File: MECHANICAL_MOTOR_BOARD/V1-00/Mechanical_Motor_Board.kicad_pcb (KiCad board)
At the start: 2 copper layers, 88.9 x 44.5 mm, 82 parts, among them K1 COLONETTE, K2 COLONETTE, K3 COLONETTE, K4 COLONETTE, P1001 CONN_02X13, P1002 CONN_02X08, P1003 CONN_01X02, P1004 CONN_01X02, P1005 CONN_01X04, P1006 CONN_01X04, Q3001 2N7002, Q3002 2N7002, Q3003 BSR14, Q3004 BSR14, Q3005 BTS50055, Q3006 BTS50055, Q3007 STB80NF55L_06T4, Q3008 STB80NF55L_06T4, Q3009 STB80NF55L_06T4, Q3010 STB80NF55L_06T4, Q3011 BTS50055, Q3012 BTS50055, Q3013 BSR14, Q3014 BSR14, Q3015 2N7002, Q3016 2N7002, U2001 HCTL-2032, U2002 M74VHC1GT02DTT1G, U3001 74HC02, U3002 74HC02, X2001 12Mhz

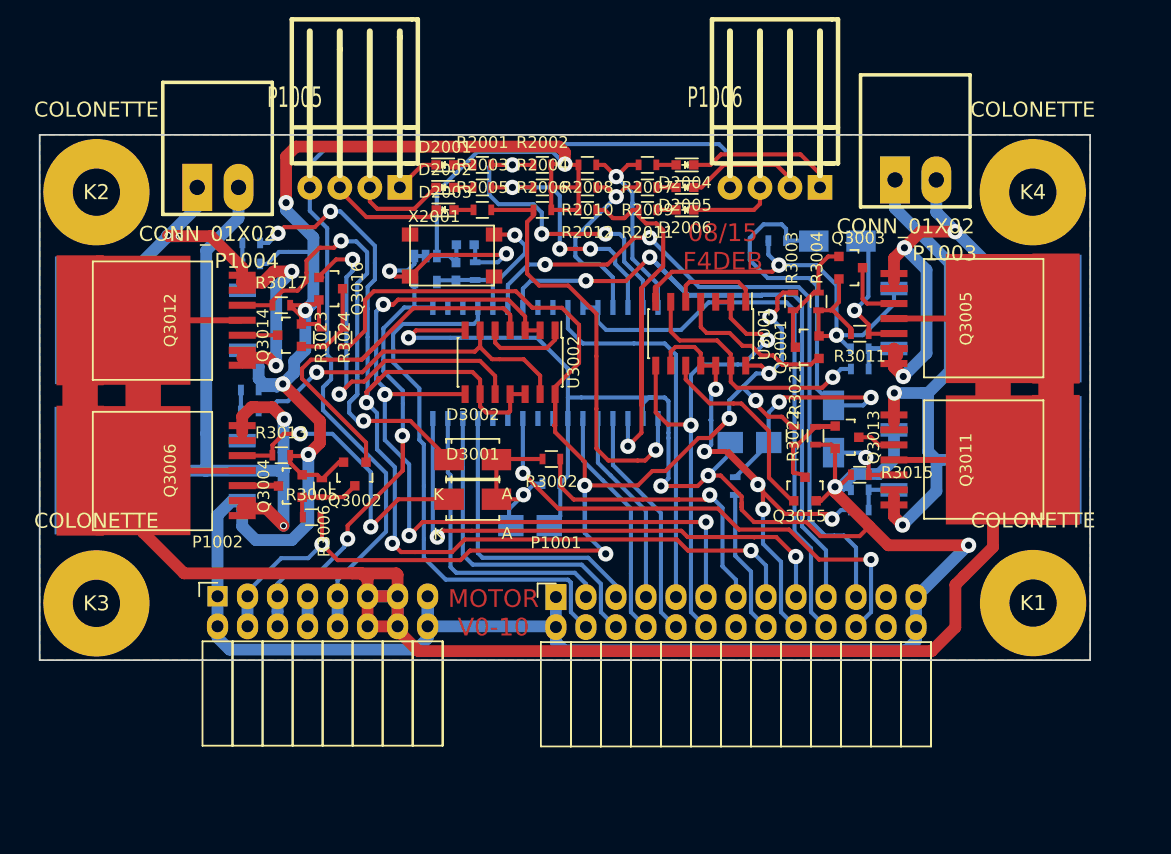
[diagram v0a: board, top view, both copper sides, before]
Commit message: test mechanicalmotorboard PCB NOK
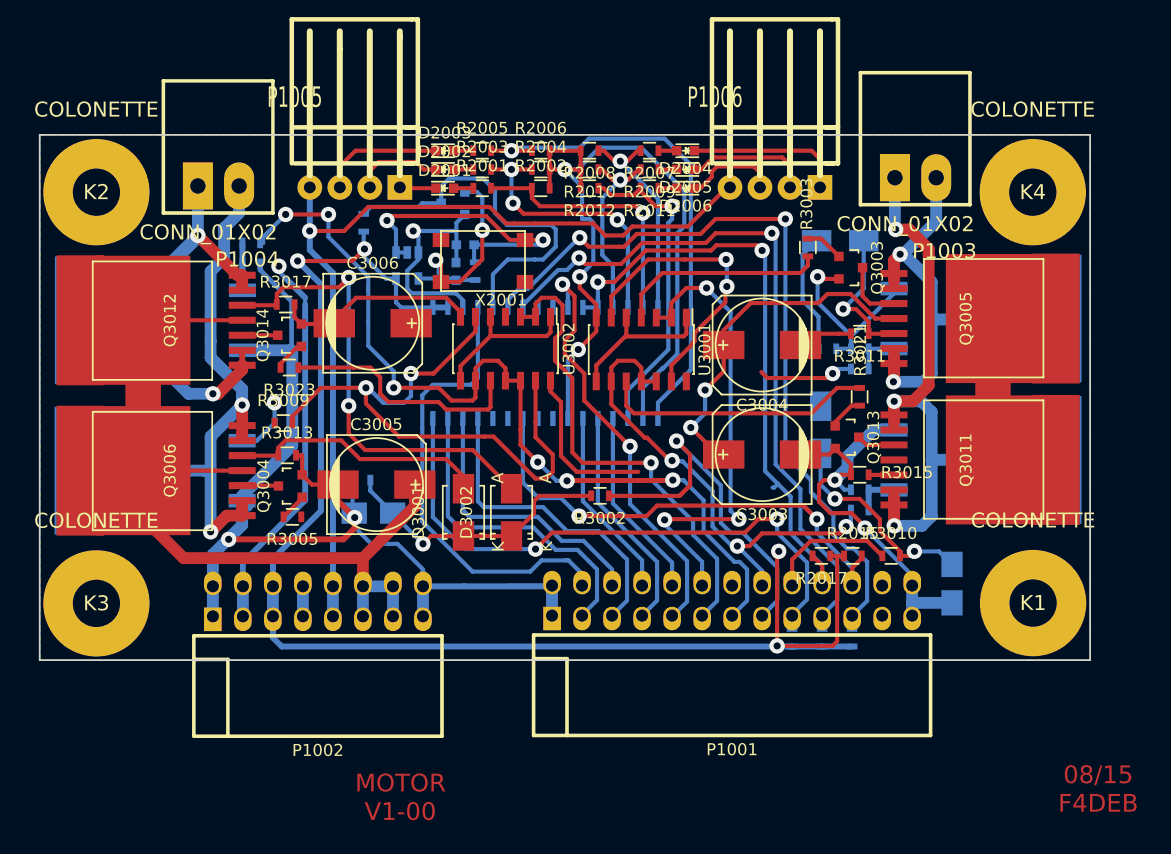
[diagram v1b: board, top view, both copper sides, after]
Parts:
- removed Q3001, Q3002, Q3015, Q3016: 2N7002, SOT-23
- removed R3004, R3006, R3022, R3024: R, Resistors_SMD:R_0603
- added C3003: 470U, c_elec_8x10.5, F.Cu at (175.4, 112.7)
- added C3004: CP, c_elec_8x10.5, F.Cu at (175.4, 103.4)
- added C3005: CP, c_elec_8x10.5, F.Cu at (142.7, 115.3)
- added C3006: CP, c_elec_8x10.5, F.Cu at (142.4, 101.6)
- added Q2001: 2N7002, Housings_SOT-23_SOT-143_TSOT-6:SOT-23, B.Cu at (149.2, 91.4)
- added R2014: 10k, Resistors_SMD:R_0603, B.Cu at (183.0, 128.2)
- added R2015: 10k, Resistors_SMD:R_0603, F.Cu at (183.1, 121.3)
- added R2016: 10k, Resistors_SMD:R_0603, B.Cu at (180.5, 128.2)
- added R2017: 10k, Resistors_SMD:R_0603, F.Cu at (180.4, 121.3)
- added R2018: 10k, Resistors_SMD:R_0603, B.Cu at (177.9, 128.2)
- added R2019: 1k, Resistors_SMD:R_0603, B.Cu at (141.7, 93.1)
- C3001, C3002: value C -> 10u
- D3001, D3002, D3003, D3004: value D_Schottky_Small -> B140
- P1001: footprint Socket_Strips:Socket_Strip_Angled_2x13 -> w_pin_strip:pin_socket_13x2-90
- P1002: footprint Socket_Strips:Socket_Strip_Angled_2x08 -> w_pin_strip:pin_socket_8x2-90
- Q3003, Q3004, Q3013, Q3014: footprint SOT-23 -> Housings_SOT-23_SOT-143_TSOT-6:SOT-23
- R2001, R2002, R2003, R2004, R2005, R2006, R2007, R2008, R2009, R2010, R2011, R2012: value 1.5k -> 2.1k
- R3001, R3007, R3012, R3014, R3016, R3018: value R -> 100k
- R3002, R3003, R3005, R3021, R3023: value R -> 10k
- R3008, R3019, R3020: value R -> 100
- R3009: value R -> 100; moved to F.Cu
- R3010: value R -> 10k; moved to F.Cu
- R3011, R3013, R3015, R3017: value R -> 2.2k
- moved C3002 20.9 mm to (191.5, 123.6), turned to 270 degrees
- moved R3001 16.1 mm to (141.5, 114.9), turned to 0 degrees
- moved P1001 15.8 mm to (172.8, 130.0)
- moved R3010 14.5 mm to (186.3, 121.3), turned to 0 degrees
- moved C3001 13.3 mm to (142.5, 117.7), turned to 180 degrees
- moved R3007 10.1 mm to (180.9, 103.8), turned to 180 degrees
- moved P1002 10.0 mm to (137.8, 130.0)
- moved R3021 6.42 mm to (183.6, 107.8)
- moved D3002 5.54 mm to (154.2, 117.6), turned to 90 degrees
- moved R3023 5.24 mm to (135.4, 105.3), turned to 180 degrees
- moved U3001 5.20 mm to (165.2, 103.8)
- moved R3002 5.16 mm to (161.7, 116.2)
- moved R2006 5.01 mm to (156.7, 87.0)
- moved D2003 5.01 mm to (148.5, 87.0)
- moved R2005 5.01 mm to (151.7, 87.0)
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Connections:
- D3001 pad 1: /Motor/IMOT2A -> Net-(C3001-Pad1)
- D3001 pad 2: Net-(C3001-Pad1) -> /Motor/IMOT2A
- D3002 pad 1: /Motor/IMOT2B -> Net-(C3001-Pad1)
- D3002 pad 2: Net-(C3001-Pad1) -> /Motor/IMOT2B
- D3003 pad 1: /Motor/IMOT1A -> Net-(C3002-Pad1)
- D3003 pad 2: Net-(C3002-Pad1) -> /Motor/IMOT1A
- D3004 pad 1: /Motor/IMOT1B -> Net-(C3002-Pad1)
- D3004 pad 2: Net-(C3002-Pad1) -> /Motor/IMOT1B
- P1001 pad 13: /Motor/IMOT2 -> /Motor/IO9
- P1001 pad 15: /Motor/IO7 -> /Motor/IMOT2
- P1001 pad 16: /Motor/IMOT1 -> /Motor/IO8
- P1001 pad 18: /Motor/IO6 -> /Motor/IMOT1
- Q3003 pad 1: Net-(Q3001-Pad3) -> Net-(Q3003-Pad1)
- Q3004 pad 1: Net-(Q3002-Pad3) -> Net-(Q3004-Pad1)
- R3003 pad 1: Net-(Q3001-Pad3) -> Net-(R3003-Pad1)
- R3003 pad 2: +3V3 -> Net-(Q3003-Pad1)
- R3005 pad 1: Net-(Q3002-Pad3) -> Net-(R3005-Pad1)
- R3005 pad 2: +3V3 -> Net-(Q3004-Pad1)
- R3019 pad 2: /Motor/IO6 -> /Motor/IO8
- R3020 pad 2: /Motor/IO7 -> /Motor/IO9
- R3021 pad 1: +3V3 -> Net-(R3021-Pad1)
- R3023 pad 1: +3V3 -> Net-(R3023-Pad1)
- U2001 pad 2: (no net) -> +5VD
- U2001 pad 3: (no net) -> GND
- U2001 pad 5: Net-(C2002-Pad1) -> Net-(Q2001-Pad3)
- U3001 pad 10: Net-(Q3015-Pad1) -> Net-(R3021-Pad1)
- U3001 pad 11: /Motor/IO6 -> /Motor/IO8
- U3001 pad 12: /Motor/IO6 -> /Motor/IO8
- U3001 pad 4: Net-(Q3001-Pad1) -> Net-(R3003-Pad1)
- U3001 pad 8: /Motor/OC5-5V -> Net-(U3001-Pad1)
- U3001 pad 9: /Motor/IO6 -> /Motor/IO8
- U3002 pad 10: Net-(Q3016-Pad1) -> Net-(R3023-Pad1)
- U3002 pad 11: /Motor/IO7 -> /Motor/IO9
- U3002 pad 12: /Motor/IO7 -> /Motor/IO9
- U3002 pad 4: Net-(Q3002-Pad1) -> Net-(R3005-Pad1)
- U3002 pad 8: /Motor/OC4-5V -> Net-(U3002-Pad1)
- U3002 pad 9: /Motor/IO7 -> /Motor/IO9
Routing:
- net GND: track 395.7 -> 278.3 mm, vias 12 -> 9
- net /Motor/IO7: track 95.6 -> 0.00 mm, vias 5 -> 0
- net +15V: track 211.7 -> 118.0 mm, vias 0 -> 2
- net +3V3: track 132.9 -> 48.8 mm, vias 7 -> 1
- net /Motor/IO9: track 0.00 -> 83.7 mm, vias 0 -> 6
- net +5VD: track 41.9 -> 125.1 mm, vias 2 -> 4
- net /Motor/IO6: track 52.1 -> 0.00 mm, vias 5 -> 0
- net /Motor/IO8: track 0.00 -> 41.6 mm, vias 0 -> 3
- net Net-(Q3002-Pad1): track 34.9 -> 0.00 mm
- net /Motor/OC4-5V: track 75.8 -> 41.3 mm, vias 4 -> 1
- net Net-(Q3016-Pad1): track 32.1 -> 0.00 mm, vias 2 -> 0
- net Net-(Q2001-Pad3): track 0.00 -> 31.8 mm
- net Net-(R3021-Pad1): track 0.00 -> 23.0 mm
- net Net-(R3023-Pad1): track 0.00 -> 20.9 mm
- net Net-(R3009-Pad2): track 30.1 -> 50.8 mm, vias 1 -> 2
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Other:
- board text added: "MOTOR V1-00"
- board text removed: "MOTOR V0-10"

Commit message: New Beacon_Main_Board
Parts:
- removed C3004, C3006: CP, c_elec_8x10.5
- C3003, C3005: footprint c_elec_8x10.5 -> Capacitors_ThroughHole:C_Axial_D13_L31_P38
- R3005: footprint Resistors_SMD:R_0603 -> Resistors_SMD:R_0805
- R3009: moved to B.Cu
- R3019, U2002: moved to F.Cu
- R3021: footprint Resistors_SMD:R_0603 -> Resistors_SMD:R_1206
- moved C3003 38.4 mm to (139.3, 99.4), turned to 0 degrees
- moved R3002 11.8 mm to (172.4, 121.0)
- moved R3001 9.60 mm to (148.8, 121.0)
- moved R3021 6.90 mm to (176.8, 107.1), turned to 0 degrees
- moved U2002 6.33 mm to (139.2, 95.2)
- moved C3001 5.72 mm to (148.2, 117.5)
- moved U2001 4.81 mm to (161.8, 105.7)
- moved C3005 3.95 mm to (139.3, 113.3)
- moved R3023 3.48 mm to (138.7, 104.5)
- moved U3001 3.02 mm to (167.5, 105.7), turned to 0 degrees
- moved D3004 2.87 mm to (181.7, 108.1), turned to 180 degrees
- moved D3002 2.54 mm to (154.2, 120.1)
- moved D3001 2.54 mm to (150.1, 120.1)
- moved R3003 2.22 mm to (181.2, 94.0), turned to 0 degrees
- moved X2001 1.84 mm to (149.9, 96.3)
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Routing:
- net +15V: track 118.0 -> 220.2 mm
- net Net-(R3005-Pad1): track 0.00 -> 53.8 mm, vias 0 -> 2
- net +3V3: track 48.8 -> 101.9 mm, vias 1 -> 3
- net GND: track 278.3 -> 322.6 mm, vias 9 -> 15
- net Net-(R2001-Pad2): track 22.2 -> 51.1 mm
- net /Motor/IMOT2: track 32.1 -> 9.34 mm
- net /Codeur/IO25: track 35.9 -> 56.6 mm
- net Net-(C2002-Pad1): track 20.0 -> 38.6 mm, vias 2 -> 1
- net Net-(R3009-Pad2): track 50.8 -> 32.3 mm, vias 2 -> 1
- net Net-(R3021-Pad1): track 23.0 -> 5.15 mm
- net Net-(U3002-Pad1): track 13.0 -> 27.3 mm, vias 0 -> 2
- net /Motor/OC5-5V: track 40.0 -> 54.0 mm, vias 3 -> 1
- net /Motor/IMOT1B: track 2.15 -> 15.3 mm, vias 0 -> 3
- net /Motor/IMOT2B: track 39.4 -> 51.6 mm, vias 2 -> 4
- net +12V: track 76.2 -> 88.2 mm, vias 1 -> 2
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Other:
- board text added: "10/15"
- board text added: "MOTOR"
- board text added: "V1-00"
- board text removed: "08/15 F4DEB"

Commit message: MAJ 2018
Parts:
- added C2001: 27p, Capacitors_SMD:C_0603, F.Cu at (73.3, 164.6)
- added C2001: 27p, Capacitors_SMD:C_0603, F.Cu at (73.8, 71.9)
- added C2001: 27p, Capacitors_SMD:C_0603, B.Cu at (208.7, 138.6)
- added C2002: 27p, Capacitors_SMD:C_0603, F.Cu at (72.5, 162.4)
- added C2002: 27p, Capacitors_SMD:C_0603, F.Cu at (73.0, 69.7)
- added C2002: 27p, Capacitors_SMD:C_0603, B.Cu at (207.9, 140.9)
- added C3001: 10u, Capacitors_Tantalum_SMD:TantalC_SizeB_EIA-3528_Wave, F.Cu at (71.2, 142.1)
- added C3001: 10u, Capacitors_Tantalum_SMD:TantalC_SizeB_EIA-3528_Wave, F.Cu at (71.8, 49.4)
- added C3001: 10u, Capacitors_Tantalum_SMD:TantalC_SizeB_EIA-3528_Wave, B.Cu at (206.6, 161.2)
- added C3002: 10u, Capacitors_Tantalum_SMD:TantalC_SizeB_EIA-3528_Wave, F.Cu at (114.5, 136.0)
- added C3002: 10u, Capacitors_Tantalum_SMD:TantalC_SizeB_EIA-3528_Wave, F.Cu at (115.0, 43.2)
- added C3002: 10u, Capacitors_Tantalum_SMD:TantalC_SizeB_EIA-3528_Wave, B.Cu at (249.9, 167.3)
- added C3003: 470U, Capacitors_ThroughHole:C_Axial_D13_L31_P38, B.Cu at (62.4, 160.1)
- added C3003: 470U, Capacitors_ThroughHole:C_Axial_D13_L31_P38, B.Cu at (62.9, 67.4)
- added C3003: 470U, Capacitors_ThroughHole:C_Axial_D13_L31_P38, F.Cu at (197.7, 143.1)
- added C3005: CP, Capacitors_ThroughHole:C_Axial_D13_L31_P38, B.Cu at (62.4, 146.3)
- added C3005: CP, Capacitors_ThroughHole:C_Axial_D13_L31_P38, B.Cu at (62.9, 53.6)
- added C3005: CP, Capacitors_ThroughHole:C_Axial_D13_L31_P38, F.Cu at (197.7, 157.0)
- added D2001: LED, LEDs:LED-0603, B.Cu at (71.6, 169.4)
- added D2001: LED, LEDs:LED-0603, B.Cu at (72.1, 76.7)
- added D2001: LED, LEDs:LED-0603, F.Cu at (206.9, 133.9)
- added D2002: LED, LEDs:LED-0603, B.Cu at (71.6, 171.0)
- added D2002: LED, LEDs:LED-0603, B.Cu at (72.1, 78.3)
- added D2002: LED, LEDs:LED-0603, F.Cu at (206.9, 132.3)
- added D2003: LED, LEDs:LED-0603, B.Cu at (71.6, 172.6)
- added D2003: LED, LEDs:LED-0603, B.Cu at (72.1, 79.9)
- added D2003: LED, LEDs:LED-0603, F.Cu at (206.9, 130.7)
- added D2004: LED, LEDs:LED-0603, B.Cu at (91.9, 172.6)
- added D2004: LED, LEDs:LED-0603, B.Cu at (92.5, 79.9)
- added D2004: LED, LEDs:LED-0603, F.Cu at (227.3, 130.7)
- added D2005: LED, LEDs:LED-0603, B.Cu at (91.9, 171.0)
- added D2005: LED, LEDs:LED-0603, B.Cu at (92.5, 78.3)
- added D2005: LED, LEDs:LED-0603, F.Cu at (227.3, 132.3)
- added D2006: LED, LEDs:LED-0603, B.Cu at (91.9, 169.4)
- added D2006: LED, LEDs:LED-0603, B.Cu at (92.5, 76.7)
- added D2006: LED, LEDs:LED-0603, F.Cu at (227.3, 133.9)
- added D3001: B140, Diodes_SMD:Diode-SMA_Standard, B.Cu at (73.2, 139.4)
- added D3001: B140, Diodes_SMD:Diode-SMA_Standard, B.Cu at (73.7, 46.7)
- added D3001: B140, Diodes_SMD:Diode-SMA_Standard, F.Cu at (208.5, 163.8)
- added D3002: B140, Diodes_SMD:Diode-SMA_Standard, B.Cu at (77.3, 139.4)
- added D3002: B140, Diodes_SMD:Diode-SMA_Standard, B.Cu at (77.8, 46.7)
- added D3002: B140, Diodes_SMD:Diode-SMA_Standard, F.Cu at (212.7, 163.8)
- added D3003: B140, Diodes_SMD:Diode-SMA_Standard, F.Cu at (104.9, 164.9)
- added D3003: B140, Diodes_SMD:Diode-SMA_Standard, F.Cu at (105.4, 72.2)
- added D3003: B140, Diodes_SMD:Diode-SMA_Standard, B.Cu at (240.3, 138.4)
- added D3004: B140, Diodes_SMD:Diode-SMA_Standard, F.Cu at (104.7, 151.5)
- added D3004: B140, Diodes_SMD:Diode-SMA_Standard, F.Cu at (105.2, 58.8)
- added D3004: B140, Diodes_SMD:Diode-SMA_Standard, B.Cu at (240.1, 151.8)
- added K1: COLONETTE, CEN-PCB:COLONETTE, B.Cu at (121.4, 134.3)
- added K1: COLONETTE, CEN-PCB:COLONETTE, B.Cu at (121.9, 41.6)
- added K1: COLONETTE, CEN-PCB:COLONETTE, F.Cu at (256.7, 169.0)
- added K2: COLONETTE, CEN-PCB:COLONETTE, B.Cu at (42.1, 169.1)
- added K2: COLONETTE, CEN-PCB:COLONETTE, B.Cu at (42.6, 76.4)
- added K2: COLONETTE, CEN-PCB:COLONETTE, F.Cu at (177.5, 134.2)
- added K3: COLONETTE, CEN-PCB:COLONETTE, B.Cu at (42.1, 134.3)
- added K3: COLONETTE, CEN-PCB:COLONETTE, B.Cu at (42.6, 41.6)
- added K3: COLONETTE, CEN-PCB:COLONETTE, F.Cu at (177.5, 169.0)
- added K4: COLONETTE, CEN-PCB:COLONETTE, B.Cu at (121.3, 169.1)
- added K4: COLONETTE, CEN-PCB:COLONETTE, B.Cu at (121.8, 76.4)
- added K4: COLONETTE, CEN-PCB:COLONETTE, F.Cu at (256.7, 134.2)
- added P1001: CONN_02X13, w_pin_strip:pin_socket_13x2-90, B.Cu at (95.9, 129.6)
- added P1001: CONN_02X13, w_pin_strip:pin_socket_13x2-90, B.Cu at (96.4, 36.9)
- added P1001: CONN_02X13, w_pin_strip:pin_socket_13x2-90, F.Cu at (231.3, 173.7)
- added P1002: CONN_02X08, w_pin_strip:pin_socket_8x2-90, B.Cu at (60.8, 129.5)
- added P1002: CONN_02X08, w_pin_strip:pin_socket_8x2-90, B.Cu at (61.3, 36.8)
- added P1002: CONN_02X08, w_pin_strip:pin_socket_8x2-90, F.Cu at (196.2, 173.7)
- added P1003: CONN_01X02, CEN-PCB:WEIDMULLER-SL-3.5-2-90G, B.Cu at (109.7, 170.3)
- added P1003: CONN_01X02, CEN-PCB:WEIDMULLER-SL-3.5-2-90G, B.Cu at (110.2, 77.6)
- added P1003: CONN_01X02, CEN-PCB:WEIDMULLER-SL-3.5-2-90G, F.Cu at (245.0, 133.0)
- added P1004: CONN_01X02, CEN-PCB:WEIDMULLER-SL-3.5-2-90G, B.Cu at (50.7, 169.6)
- added P1004: CONN_01X02, CEN-PCB:WEIDMULLER-SL-3.5-2-90G, B.Cu at (51.2, 76.9)
- added P1004: CONN_01X02, CEN-PCB:WEIDMULLER-SL-3.5-2-90G, F.Cu at (186.1, 133.7)
- added P1005: CONN_01X04, CEN-PCB:KK-4-H, B.Cu at (60.1, 169.5)
- added P1005: CONN_01X04, CEN-PCB:KK-4-H, B.Cu at (60.7, 76.8)
- added P1005: CONN_01X04, CEN-PCB:KK-4-H, F.Cu at (195.5, 133.8)
- added P1006: CONN_01X04, CEN-PCB:KK-4-H, B.Cu at (95.7, 169.5)
- added P1006: CONN_01X04, CEN-PCB:KK-4-H, B.Cu at (96.2, 76.8)
- added P1006: CONN_01X04, CEN-PCB:KK-4-H, F.Cu at (231.1, 133.8)
- added Q2001: 2N7002, Housings_SOT-23_SOT-143_TSOT-6:SOT-23, F.Cu at (72.3, 168.1)
- added Q2001: 2N7002, Housings_SOT-23_SOT-143_TSOT-6:SOT-23, F.Cu at (72.8, 75.4)
- added Q2001: 2N7002, Housings_SOT-23_SOT-143_TSOT-6:SOT-23, B.Cu at (207.6, 135.1)
- added Q3003: BSR14, Housings_SOT-23_SOT-143_TSOT-6:SOT-23, B.Cu at (105.9, 162.7)
- added Q3003: BSR14, Housings_SOT-23_SOT-143_TSOT-6:SOT-23, B.Cu at (106.4, 70.0)
- added Q3003: BSR14, Housings_SOT-23_SOT-143_TSOT-6:SOT-23, F.Cu at (241.3, 140.6)
- added Q3004: BSR14, Housings_SOT-23_SOT-143_TSOT-6:SOT-23, B.Cu at (58.5, 143.9)
- added Q3004: BSR14, Housings_SOT-23_SOT-143_TSOT-6:SOT-23, B.Cu at (59.0, 51.2)
- added Q3004: BSR14, Housings_SOT-23_SOT-143_TSOT-6:SOT-23, F.Cu at (193.9, 159.4)
- added Q3005: BTS50055, f4deb-mod-library:PG-TO220-7-4, B.Cu at (109.6, 158.4)
- added Q3005: BTS50055, f4deb-mod-library:PG-TO220-7-4, B.Cu at (110.1, 65.7)
- added Q3005: BTS50055, f4deb-mod-library:PG-TO220-7-4, F.Cu at (245.0, 144.9)
- added Q3006: BTS50055, f4deb-mod-library:PG-TO220-7-4, B.Cu at (54.4, 145.5)
- added Q3006: BTS50055, f4deb-mod-library:PG-TO220-7-4, B.Cu at (54.9, 52.8)
- added Q3006: BTS50055, f4deb-mod-library:PG-TO220-7-4, F.Cu at (189.8, 157.8)
- added Q3007: STB80NF55L_06T4, SMD_Packages:TO-263, F.Cu at (109.6, 158.4)
- added Q3007: STB80NF55L_06T4, SMD_Packages:TO-263, F.Cu at (110.1, 65.7)
- added Q3007: STB80NF55L_06T4, SMD_Packages:TO-263, B.Cu at (245.0, 144.9)
- added Q3008: STB80NF55L_06T4, SMD_Packages:TO-263, F.Cu at (54.4, 145.5)
- added Q3008: STB80NF55L_06T4, SMD_Packages:TO-263, F.Cu at (54.9, 52.8)
- added Q3008: STB80NF55L_06T4, SMD_Packages:TO-263, B.Cu at (189.8, 157.8)
- added Q3009: STB80NF55L_06T4, SMD_Packages:TO-263, F.Cu at (109.6, 146.4)
- added Q3009: STB80NF55L_06T4, SMD_Packages:TO-263, F.Cu at (110.1, 53.7)
- added Q3009: STB80NF55L_06T4, SMD_Packages:TO-263, B.Cu at (245.0, 156.9)
- added Q3010: STB80NF55L_06T4, SMD_Packages:TO-263, F.Cu at (54.4, 158.2)
- added Q3010: STB80NF55L_06T4, SMD_Packages:TO-263, F.Cu at (55.0, 65.5)
- added Q3010: STB80NF55L_06T4, SMD_Packages:TO-263, B.Cu at (189.8, 145.0)
- added Q3011: BTS50055, f4deb-mod-library:PG-TO220-7-4, B.Cu at (109.6, 146.4)
- added Q3011: BTS50055, f4deb-mod-library:PG-TO220-7-4, B.Cu at (110.1, 53.7)
- added Q3011: BTS50055, f4deb-mod-library:PG-TO220-7-4, F.Cu at (245.0, 156.9)
- added Q3012: BTS50055, f4deb-mod-library:PG-TO220-7-4, B.Cu at (54.4, 158.2)
- added Q3012: BTS50055, f4deb-mod-library:PG-TO220-7-4, B.Cu at (54.9, 65.5)
- added Q3012: BTS50055, f4deb-mod-library:PG-TO220-7-4, F.Cu at (189.8, 145.0)
- added Q3013: BSR14, Housings_SOT-23_SOT-143_TSOT-6:SOT-23, B.Cu at (105.6, 148.3)
- added Q3013: BSR14, Housings_SOT-23_SOT-143_TSOT-6:SOT-23, B.Cu at (106.1, 55.6)
- added Q3013: BSR14, Housings_SOT-23_SOT-143_TSOT-6:SOT-23, F.Cu at (241.0, 154.9)
- added Q3014: BSR14, Housings_SOT-23_SOT-143_TSOT-6:SOT-23, B.Cu at (58.5, 156.1)
- added Q3014: BSR14, Housings_SOT-23_SOT-143_TSOT-6:SOT-23, B.Cu at (59.0, 63.4)
- added Q3014: BSR14, Housings_SOT-23_SOT-143_TSOT-6:SOT-23, F.Cu at (193.9, 147.2)
- added R2001: 2.1k, Resistors_SMD:R_0603, B.Cu at (74.7, 169.4)
- added R2001: 2.1k, Resistors_SMD:R_0603, B.Cu at (75.2, 76.7)
- added R2001: 2.1k, Resistors_SMD:R_0603, F.Cu at (210.1, 133.9)
- added R2002: 2.1k, Resistors_SMD:R_0603, B.Cu at (79.7, 169.4)
- added R2002: 2.1k, Resistors_SMD:R_0603, B.Cu at (80.2, 76.7)
- added R2002: 2.1k, Resistors_SMD:R_0603, F.Cu at (215.1, 133.9)
- added R2003: 2.1k, Resistors_SMD:R_0603, B.Cu at (74.7, 171.0)
- added R2003: 2.1k, Resistors_SMD:R_0603, B.Cu at (75.2, 78.3)
- added R2003: 2.1k, Resistors_SMD:R_0603, F.Cu at (210.1, 132.3)
- added R2004: 2.1k, Resistors_SMD:R_0603, B.Cu at (79.7, 171.0)
- added R2004: 2.1k, Resistors_SMD:R_0603, B.Cu at (80.2, 78.3)
- added R2004: 2.1k, Resistors_SMD:R_0603, F.Cu at (215.1, 132.3)
- added R2005: 2.1k, Resistors_SMD:R_0603, B.Cu at (74.7, 172.6)
- added R2005: 2.1k, Resistors_SMD:R_0603, B.Cu at (75.2, 79.9)
- added R2005: 2.1k, Resistors_SMD:R_0603, F.Cu at (210.1, 130.7)
- added R2006: 2.1k, Resistors_SMD:R_0603, B.Cu at (79.7, 172.6)
- added R2006: 2.1k, Resistors_SMD:R_0603, B.Cu at (80.2, 79.9)
- added R2006: 2.1k, Resistors_SMD:R_0603, F.Cu at (215.1, 130.7)
- added R2007: 2.1k, Resistors_SMD:R_0603, B.Cu at (88.9, 172.6)
- added R2007: 2.1k, Resistors_SMD:R_0603, B.Cu at (89.4, 79.9)
- added R2007: 2.1k, Resistors_SMD:R_0603, F.Cu at (224.3, 130.7)
- added R2008: 2.1k, Resistors_SMD:R_0603, B.Cu at (83.8, 172.6)
- added R2008: 2.1k, Resistors_SMD:R_0603, B.Cu at (84.3, 79.9)
- added R2008: 2.1k, Resistors_SMD:R_0603, F.Cu at (219.2, 130.7)
- added R2009: 2.1k, Resistors_SMD:R_0603, B.Cu at (88.9, 171.0)
- added R2009: 2.1k, Resistors_SMD:R_0603, B.Cu at (89.4, 78.3)
- added R2009: 2.1k, Resistors_SMD:R_0603, F.Cu at (224.3, 132.3)
- added R2010: 2.1k, Resistors_SMD:R_0603, B.Cu at (83.8, 171.0)
- added R2010: 2.1k, Resistors_SMD:R_0603, B.Cu at (84.3, 78.3)
- added R2010: 2.1k, Resistors_SMD:R_0603, F.Cu at (219.2, 132.3)
- added R2011: 2.1k, Resistors_SMD:R_0603, B.Cu at (88.9, 169.4)
- added R2011: 2.1k, Resistors_SMD:R_0603, B.Cu at (89.4, 76.7)
- added R2011: 2.1k, Resistors_SMD:R_0603, F.Cu at (224.3, 133.9)
- added R2012: 2.1k, Resistors_SMD:R_0603, B.Cu at (83.8, 169.4)
- added R2012: 2.1k, Resistors_SMD:R_0603, B.Cu at (84.3, 76.7)
- added R2012: 2.1k, Resistors_SMD:R_0603, F.Cu at (219.2, 133.9)
- added R2013: 10M, Resistors_SMD:R_0603, F.Cu at (74.1, 162.4)
- added R2013: 10M, Resistors_SMD:R_0603, F.Cu at (74.6, 69.7)
- added R2013: 10M, Resistors_SMD:R_0603, B.Cu at (209.5, 140.9)
- added R2014: 10k, Resistors_SMD:R_0603, F.Cu at (106.0, 131.4)
- added R2014: 10k, Resistors_SMD:R_0603, F.Cu at (106.6, 38.7)
- added R2014: 10k, Resistors_SMD:R_0603, B.Cu at (241.4, 171.9)
- added R2015: 10k, Resistors_SMD:R_0603, B.Cu at (106.8, 138.3)
- added R2015: 10k, Resistors_SMD:R_0603, B.Cu at (107.3, 45.6)
- added R2015: 10k, Resistors_SMD:R_0603, F.Cu at (242.2, 165.0)
- added R2016: 10k, Resistors_SMD:R_0603, F.Cu at (103.5, 131.4)
- added R2016: 10k, Resistors_SMD:R_0603, F.Cu at (104.0, 38.7)
- added R2016: 10k, Resistors_SMD:R_0603, B.Cu at (238.9, 171.9)
- added R2017: 10k, Resistors_SMD:R_0603, B.Cu at (102.7, 138.3)
- added R2017: 10k, Resistors_SMD:R_0603, B.Cu at (103.3, 45.6)
- added R2017: 10k, Resistors_SMD:R_0603, F.Cu at (238.1, 165.0)
- added R2018: 10k, Resistors_SMD:R_0603, F.Cu at (101.0, 131.4)
- added R2018: 10k, Resistors_SMD:R_0603, F.Cu at (101.5, 38.7)
- added R2018: 10k, Resistors_SMD:R_0603, B.Cu at (236.3, 171.9)
- added R2019: 1k, Resistors_SMD:R_0603, F.Cu at (64.7, 166.5)
- added R2019: 1k, Resistors_SMD:R_0603, F.Cu at (65.2, 73.8)
- added R2019: 1k, Resistors_SMD:R_0603, B.Cu at (200.1, 136.8)
- added R3001: 100k, Resistors_SMD:R_0603, F.Cu at (71.9, 138.6)
- added R3001: 100k, Resistors_SMD:R_0603, F.Cu at (72.4, 45.8)
- added R3001: 100k, Resistors_SMD:R_0603, B.Cu at (207.3, 164.7)
- added R3002: 10k, Resistors_SMD:R_0603, B.Cu at (95.4, 138.6)
- added R3002: 10k, Resistors_SMD:R_0603, B.Cu at (95.9, 45.8)
- added R3002: 10k, Resistors_SMD:R_0603, F.Cu at (230.8, 164.7)
- added R3003: 10k, Resistors_SMD:R_0603, B.Cu at (104.2, 165.5)
- added R3003: 10k, Resistors_SMD:R_0603, B.Cu at (104.7, 72.8)
- added R3003: 10k, Resistors_SMD:R_0603, F.Cu at (239.6, 137.7)
- added R3005: 10k, Resistors_SMD:R_0805, B.Cu at (59.4, 140.6)
- added R3005: 10k, Resistors_SMD:R_0805, B.Cu at (59.9, 47.9)
- added R3005: 10k, Resistors_SMD:R_0805, F.Cu at (194.8, 162.7)
- added R3007: 100k, Resistors_SMD:R_0603, F.Cu at (103.9, 155.8)
- added R3007: 100k, Resistors_SMD:R_0603, F.Cu at (104.5, 63.1)
- added R3007: 100k, Resistors_SMD:R_0603, B.Cu at (239.3, 147.4)
- added R3008: 100, Resistors_SMD:R_0603, F.Cu at (106.7, 154.1)
- added R3008: 100, Resistors_SMD:R_0603, F.Cu at (107.2, 61.4)
- added R3008: 100, Resistors_SMD:R_0603, B.Cu at (242.1, 149.2)
- added R3009: 100, Resistors_SMD:R_0603, F.Cu at (58.7, 150.6)
- added R3009: 100, Resistors_SMD:R_0603, F.Cu at (59.2, 57.9)
- added R3009: 100, Resistors_SMD:R_0603, B.Cu at (194.1, 152.7)
- added R3010: 10k, Resistors_SMD:R_0603, B.Cu at (109.3, 138.3)
- added R3010: 10k, Resistors_SMD:R_0603, B.Cu at (109.9, 45.6)
- added R3010: 10k, Resistors_SMD:R_0603, F.Cu at (244.7, 165.0)
- added R3011: 2.2k, Resistors_SMD:R_0603, B.Cu at (106.7, 157.4)
- added R3011: 2.2k, Resistors_SMD:R_0603, B.Cu at (107.2, 64.6)
- added R3011: 2.2k, Resistors_SMD:R_0603, F.Cu at (242.1, 145.9)
- added R3012: 100k, Resistors_SMD:R_0603, F.Cu at (106.7, 155.8)
- added R3012: 100k, Resistors_SMD:R_0603, F.Cu at (107.2, 63.1)
- added R3012: 100k, Resistors_SMD:R_0603, B.Cu at (242.1, 147.4)
- added R3013: 2.2k, Resistors_SMD:R_0603, B.Cu at (58.7, 147.0)
- added R3013: 2.2k, Resistors_SMD:R_0603, B.Cu at (59.2, 54.3)
- added R3013: 2.2k, Resistors_SMD:R_0603, F.Cu at (194.1, 156.3)
- added R3014: 100k, Resistors_SMD:R_0603, F.Cu at (58.7, 148.8)
- added R3014: 100k, Resistors_SMD:R_0603, F.Cu at (59.2, 56.1)
- added R3014: 100k, Resistors_SMD:R_0603, B.Cu at (194.1, 154.4)
- added R3015: 2.2k, Resistors_SMD:R_0603, B.Cu at (105.3, 145.5)
- added R3015: 2.2k, Resistors_SMD:R_0603, B.Cu at (105.8, 52.8)
- added R3015: 2.2k, Resistors_SMD:R_0603, F.Cu at (240.7, 157.8)
- added R3016: 100k, Resistors_SMD:R_0603, F.Cu at (106.7, 143.9)
- added R3016: 100k, Resistors_SMD:R_0603, F.Cu at (107.2, 51.2)
- added R3016: 100k, Resistors_SMD:R_0603, B.Cu at (242.1, 159.4)
- added R3017: 2.2k, Resistors_SMD:R_0603, B.Cu at (58.9, 159.5)
- added R3017: 2.2k, Resistors_SMD:R_0603, B.Cu at (59.4, 66.8)
- added R3017: 2.2k, Resistors_SMD:R_0603, F.Cu at (194.2, 143.8)
- added R3018: 100k, Resistors_SMD:R_0603, F.Cu at (55.2, 163.0)
- added R3018: 100k, Resistors_SMD:R_0603, F.Cu at (55.7, 70.3)
- added R3018: 100k, Resistors_SMD:R_0603, B.Cu at (190.6, 140.3)
- added R3019: 100, Resistors_SMD:R_0603, B.Cu at (106.7, 143.9)
- added R3019: 100, Resistors_SMD:R_0603, B.Cu at (107.2, 51.2)
- added R3019: 100, Resistors_SMD:R_0603, F.Cu at (242.1, 159.4)
- added R3020: 100, Resistors_SMD:R_0603, F.Cu at (55.2, 164.8)
- added R3020: 100, Resistors_SMD:R_0603, F.Cu at (55.7, 72.1)
- added R3020: 100, Resistors_SMD:R_0603, B.Cu at (190.6, 138.5)
- added R3021: 10k, Resistors_SMD:R_1206, B.Cu at (99.8, 152.5)
- added R3021: 10k, Resistors_SMD:R_1206, B.Cu at (100.3, 59.8)
- added R3021: 10k, Resistors_SMD:R_1206, F.Cu at (235.2, 150.7)
- added R3023: 10k, Resistors_SMD:R_0603, B.Cu at (61.8, 155.1)
- added R3023: 10k, Resistors_SMD:R_0603, B.Cu at (62.3, 62.4)
- added R3023: 10k, Resistors_SMD:R_0603, F.Cu at (197.2, 148.1)
- added U2001: HCTL-2032, SMD_Packages:SOJ-32, F.Cu at (84.8, 153.9)
- added U2001: HCTL-2032, SMD_Packages:SOJ-32, F.Cu at (85.3, 61.2)
- added U2001: HCTL-2032, SMD_Packages:SOJ-32, B.Cu at (220.2, 149.4)
- added U2002: M74VHC1GT02DTT1G, Housings_SOT-23_SOT-143_TSOT-6:SOT-23-5, B.Cu at (62.2, 164.3)
- added U2002: M74VHC1GT02DTT1G, Housings_SOT-23_SOT-143_TSOT-6:SOT-23-5, B.Cu at (62.7, 71.6)
- added U2002: M74VHC1GT02DTT1G, Housings_SOT-23_SOT-143_TSOT-6:SOT-23-5, F.Cu at (197.6, 138.9)
- added U3001: 74HC02, Housings_SOIC:SOIC-14_3.9x8.7mm_Pitch1.27mm, B.Cu at (90.6, 153.9)
- added U3001: 74HC02, Housings_SOIC:SOIC-14_3.9x8.7mm_Pitch1.27mm, B.Cu at (91.1, 61.2)
- added U3001: 74HC02, Housings_SOIC:SOIC-14_3.9x8.7mm_Pitch1.27mm, F.Cu at (225.9, 149.4)
- added U3002: 74HC02, Housings_SOIC:SOIC-14_3.9x8.7mm_Pitch1.27mm, B.Cu at (76.7, 155.8)
- added U3002: 74HC02, Housings_SOIC:SOIC-14_3.9x8.7mm_Pitch1.27mm, B.Cu at (77.2, 63.1)
- added U3002: 74HC02, Housings_SOIC:SOIC-14_3.9x8.7mm_Pitch1.27mm, F.Cu at (212.1, 147.4)
- added X2001: 12Mhz, f4deb-mod-library:MDX75104, B.Cu at (73.0, 163.3)
- added X2001: 12Mhz, f4deb-mod-library:MDX75104, B.Cu at (73.5, 70.6)
- added X2001: 12Mhz, f4deb-mod-library:MDX75104, F.Cu at (208.3, 140.0)
- moved C2001 75.9 mm to (208.2, 45.9)
- moved C3002 75.9 mm to (249.4, 74.6)
- moved C3003 75.9 mm to (197.2, 50.4)
- moved C3005 75.9 mm to (197.2, 64.3)
- moved D2003 75.9 mm to (206.4, 38.0)
- moved D2004 75.9 mm to (226.8, 38.0)
- moved K1 75.9 mm to (256.2, 76.3)
- moved P1002 75.9 mm to (195.7, 81.0)
- moved P1003 75.9 mm to (244.5, 40.3)
- moved P1005 75.9 mm to (195.0, 41.1)
- moved P1006 75.9 mm to (230.6, 41.1)
- moved Q3006 75.9 mm to (189.3, 65.1)
- moved Q3008 75.9 mm to (189.3, 65.1)
- moved R2007 75.9 mm to (223.8, 38.0)
- moved R2014 75.9 mm to (240.9, 79.2)
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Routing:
- net GND: track 322.6 -> 1292.9 mm, vias 15 -> 60
- net +15V: track 220.2 -> 880.7 mm, vias 2 -> 8
- net +5VD: track 132.1 -> 570.5 mm, vias 4 -> 16
- net +3V3: track 101.9 -> 407.7 mm, vias 3 -> 12
- net +12V: track 88.2 -> 352.9 mm, vias 2 -> 8
- net /Motor/IO9: track 76.7 -> 315.9 mm, vias 4 -> 16
- net Net-(C3002-Pad1): track 40.3 -> 250.9 mm, vias 3 -> 12
- net /Codeur/IO1: track 64.4 -> 257.6 mm, vias 2 -> 8
- net /Codeur/IO4: track 60.4 -> 247.5 mm, vias 2 -> 8
- net /Motor/M1B: track 61.9 -> 247.7 mm, vias 2 -> 8
- net /Codeur/IO25: track 56.6 -> 219.9 mm, vias 2 -> 8
- net /Motor/M2A: track 54.4 -> 217.7 mm, vias 2 -> 8
- net /Codeur/IO3: track 57.3 -> 220.5 mm, vias 4 -> 16
- net /Motor/OC5-5V: track 54.0 -> 216.1 mm, vias 1 -> 4
- net Net-(R3005-Pad1): track 53.8 -> 214.1 mm, vias 2 -> 8
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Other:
- board size 88.9 x 44.5 mm -> 224.3 x 137.3 mm
- board text added: "02/18"
- board text added: "V1-10"
- board text removed: "10/15"
- board text removed: "MOTOR V1-00"
- board text removed: "V1-00"
